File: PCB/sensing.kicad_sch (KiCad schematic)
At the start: 2 parts

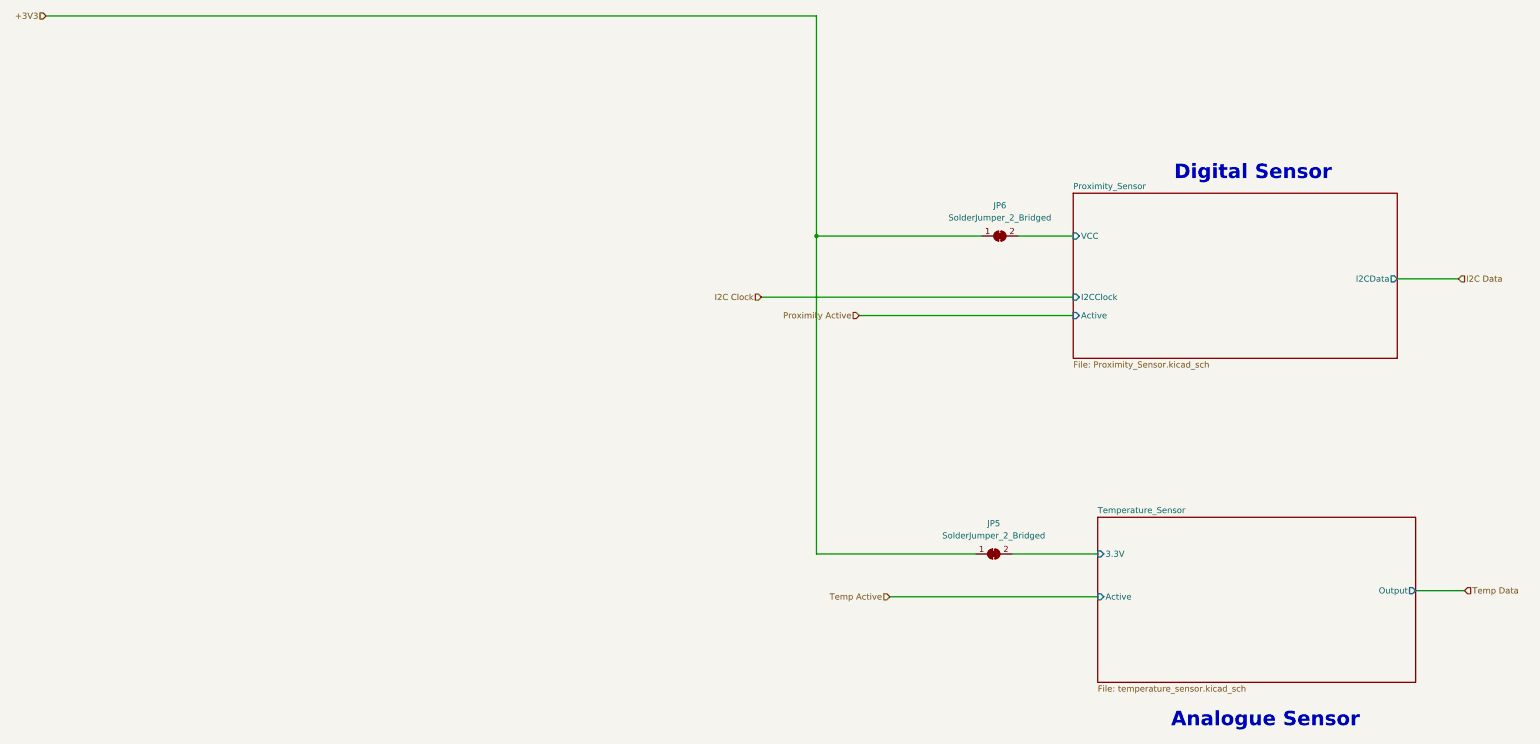
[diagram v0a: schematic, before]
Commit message: Mostly addressed issues with Sensing subsystem
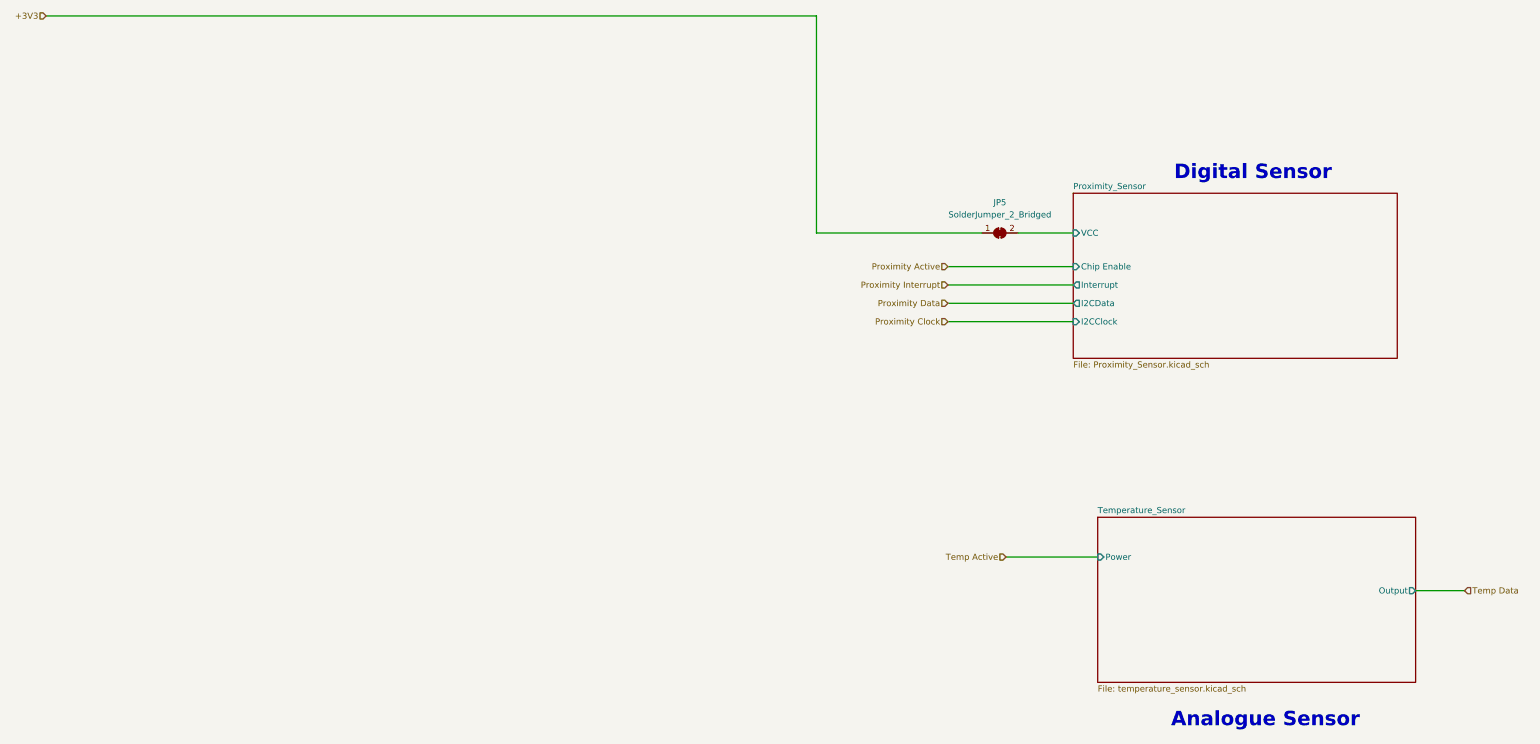
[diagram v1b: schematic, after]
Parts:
- removed JP5: SolderJumper_2_Bridged, Jumper:SolderJumper-2_P1.3mm_Bridged2Bar_Pad1.0x1.5mm, symbol Jumper:SolderJumper_2_Bridged
- renumbered JP6 to JP5
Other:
- sheet Proximity_Sensor ports: added Chip Enable, Interrupt; removed Active
- sheet Temperature_Sensor ports: added Power; removed 3.3V, Active
- moved on the sheet: JP5
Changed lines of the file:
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@@
     (comment 4 "Authors: Kelvin Yankey")
-  )
-  (junction (at 196.85 92.71) (diameter 0) (color 0 0 0 0)
   )
   (wire (pts (xy 321.31 166.37) (xy 331.47 166.37))
     (stroke (width 0) (type default) (color 0 0 0 0))
   )
-  (wire (pts (xy 238.76 92.71) (xy 250.19 92.71))
+  (wire (pts (xy 238.76 92.075) (xy 250.19 92.075))
     (stroke (width 0) (type default) (color 0 0 0 0))
   )
-  (wire (pts (xy 185.42 105.41) (xy 250.19 105.41))
+  (wire (pts (xy 236.22 159.385) (xy 255.27 159.385))
     (stroke (width 0) (type default) (color 0 0 0 0))
   )
-  (wire (pts (xy 212.09 167.64) (xy 255.27 167.64))
-    (stroke (width 0) (type default) (color 0 0 0 0))
-  )
-  (wire (pts (xy 317.5 101.6) (xy 330.2 101.6))
-    (stroke (width 0) (type default) (color 0 0 0 0))
-  )
-  (wire (pts (xy 196.85 158.75) (xy 196.85 92.71))
+  (wire (pts (xy 224.155 102.87) (xy 250.19 102.87))
     (stroke (width 0) (type default) (color 0 0 0 0))
   )
@@
     (stroke (width 0) (type default) (color 0 0 0 0))
   )
-  (wire (pts (xy 229.87 158.75) (xy 196.85 158.75))
+  (wire (pts (xy 224.155 99.06) (xy 250.19 99.06))
     (stroke (width 0) (type default) (color 0 0 0 0))
   )
-  (wire (pts (xy 237.49 158.75) (xy 255.27 158.75))
+  (wire (pts (xy 224.155 106.68) (xy 250.19 106.68))
     (stroke (width 0) (type default) (color 0 0 0 0))
   )
-  (wire (pts (xy 196.85 92.71) (xy 196.85 46.99))
+  (wire (pts (xy 224.155 110.49) (xy 250.19 110.49))
     (stroke (width 0) (type default) (color 0 0 0 0))
   )
-  (wire (pts (xy 196.85 92.71) (xy 231.14 92.71))
+  (wire (pts (xy 196.85 92.075) (xy 196.85 46.99))
     (stroke (width 0) (type default) (color 0 0 0 0))
   )
-  (wire (pts (xy 205.74 109.22) (xy 250.19 109.22))
+  (wire (pts (xy 196.85 92.075) (xy 231.14 92.075))
     (stroke (width 0) (type default) (color 0 0 0 0))
   )
@@
     (effects (font (size 3 3) (thickness 0.6) bold) (justify left bottom))
   )
+  (hierarchical_label "Proximity Active" (shape input) (at 224.155 99.06 180)
+    (effects (font (size 1.27 1.27)) (justify right))
+  )
+  (hierarchical_label "Temp Active" (shape input) (at 236.22 159.385 180)
+    (effects (font (size 1.27 1.27)) (justify right))
+  )
+  (hierarchical_label "Proximity Clock" (shape input) (at 224.155 110.49 180)
+    (effects (font (size 1.27 1.27)) (justify right))
+  )
+  (hierarchical_label "Proximity Data" (shape input) (at 224.155 106.68 180)
+    (effects (font (size 1.27 1.27)) (justify right))
+  )
   (hierarchical_label "Temp Data" (shape input) (at 331.47 166.37 0)
     (effects (font (size 1.27 1.27)) (justify left))
   )
-  (hierarchical_label "I2C Clock" (shape input) (at 185.42 105.41 180)
+  (hierarchical_label "Proximity Interrupt" (shape input) (at 224.155 102.87 180)
     (effects (font (size 1.27 1.27)) (justify right))
-  )
-  (hierarchical_label "Temp Active" (shape input) (at 212.09 167.64 180)
-    (effects (font (size 1.27 1.27)) (justify right))
-  )
-  (hierarchical_label "Proximity Active" (shape input) (at 205.74 109.22 180)
-    (effects (font (size 1.27 1.27)) (justify right))
-  )
-  (hierarchical_label "I2C Data" (shape input) (at 330.2 101.6 0)
-    (effects (font (size 1.27 1.27)) (justify left))
   )
   (hierarchical_label "+3V3" (shape input) (at 36.83 46.99 180)
     (effects (font (size 1.27 1.27)) (justify right))
   )
-  (symbol (lib_id "Jumper:SolderJumper_2_Bridged") (at 234.95 92.71 0) (unit 1)
+  (symbol (lib_id "Jumper:SolderJumper_2_Bridged") (at 234.95 92.075 0) (unit 1)
     (in_bom yes) (on_board yes) (fields_autoplaced)
-    (property "Reference" "JP6" (id 0) (at 234.95 86.36 0))
-    (property "Value" "SolderJumper_2_Bridged" (id 1) (at 234.95 88.9 0))
-    (property "Footprint" "Jumper:SolderJumper-2_P1.3mm_Bridged2Bar_Pad1.0x1.5mm" (id 2) (at 234.95 92.71 0)
+    (property "Reference" "JP5" (id 0) (at 234.95 85.725 0))
+    (property "Value" "SolderJumper_2_Bridged" (id 1) (at 234.95 88.265 0))
+    (property "Footprint" "Jumper:SolderJumper-2_P1.3mm_Bridged2Bar_Pad1.0x1.5mm" (id 2) (at 234.95 92.075 0)
       (effects (font (size 1.27 1.27)) hide)
     )
-    (property "Datasheet" "~" (id 3) (at 234.95 92.71 0)
-      (effects (font (size 1.27 1.27)) hide)
-    )
-    (pin "1")
-    (pin "2")
-  )
-  (symbol (lib_id "Jumper:SolderJumper_2_Bridged") (at 233.68 158.75 0) (unit 1)
-    (in_bom yes) (on_board yes) (fields_autoplaced)
-    (property "Reference" "JP5" (id 0) (at 233.68 152.4 0))
-    (property "Value" "SolderJumper_2_Bridged" (id 1) (at 233.68 154.94 0))
-    (property "Footprint" "Jumper:SolderJumper-2_P1.3mm_Bridged2Bar_Pad1.0x1.5mm" (id 2) (at 233.68 158.75 0)
-      (effects (font (size 1.27 1.27)) hide)
-    )
-    (property "Datasheet" "~" (id 3) (at 233.68 158.75 0)
+    (property "Datasheet" "~" (id 3) (at 234.95 92.075 0)
       (effects (font (size 1.27 1.27)) hide)
     )
@@
       (effects (font (size 1.27 1.27)) (justify left top))
     )
-    (pin "VCC" input (at 250.19 92.71 180)
+    (pin "Chip Enable" input (at 250.19 99.06 180)
       (effects (font (size 1.27 1.27)) (justify left))
     )
-    (pin "Active" input (at 250.19 109.22 180)
+    (pin "I2CClock" input (at 250.19 110.49 180)
       (effects (font (size 1.27 1.27)) (justify left))
     )
-    (pin "I2CClock" input (at 250.19 105.41 180)
+    (pin "Interrupt" output (at 250.19 102.87 180)
       (effects (font (size 1.27 1.27)) (justify left))
     )
-    (pin "I2CData" output (at 317.5 101.6 0)
-      (effects (font (size 1.27 1.27)) (justify right))
+    (pin "I2CData" output (at 250.19 106.68 180)
+      (effects (font (size 1.27 1.27)) (justify left))
+    )
+    (pin "VCC" input (at 250.19 92.075 180)
+      (effects (font (size 1.27 1.27)) (justify left))
     )
   )
@@
       (effects (font (size 1.27 1.27)) (justify right))
     )
-    (pin "3.3V" input (at 255.27 158.75 180)
+    (pin "Power" input (at 255.27 159.385 180)
       (effects (font (size 1.27 1.27)) (justify left))
     )
-    (pin "Active" input (at 255.27 167.64 180)
-      (effects (font (size 1.27 1.27)) (justify left))
-    )
